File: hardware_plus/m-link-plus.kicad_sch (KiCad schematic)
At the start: 31 parts, among them J3 SIG, J4 PROGRAM, J5 I2C, SW1 RESTORE SETTINGS, U1 AP1117-33, U2 DRV8837C, U3 DRV8837C, U4 ESP-12F, U5 PCA9685PW, U6 DRV8837C

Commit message: Rework M-Link Plus by swapping the PCA9865 and the regulator.
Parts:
- removed R6, R8: 10k, Resistor_SMD:R_0603_1608Metric, symbol Device:R
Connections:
- net CH6: now also U5.15 (LED8); no longer U5.18 (LED11)
- net CH7: now also U5.16 (LED9); no longer U5.17 (LED10)
- net CH8: now also U5.17 (LED10); no longer U5.16 (LED9)
- net CH9: now also U5.18 (LED11); no longer U5.15 (LED8)
- net MTDI: no longer names the net of U4.16 (GPIO15)
- net OE: no longer names the net of U4.17 (GPIO2)
- no-connect marks 16 -> 18
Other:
- note added: "MTDI"
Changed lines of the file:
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@@
   (junction (at 157.48 217.17) (diameter 0) (color 0 0 0 0)
   )
-  (junction (at 184.15 97.79) (diameter 0) (color 0 0 0 0)
-  )
   (junction (at 64.77 262.89) (diameter 0) (color 0 0 0 0)
   )
@@
   )
   (junction (at 97.79 36.83) (diameter 0) (color 0 0 0 0)
-  )
-  (junction (at 189.23 36.83) (diameter 0) (color 0 0 0 0)
   )
   (junction (at 38.1 144.78) (diameter 0) (color 0 0 0 0)
@@
   (no_connect (at 143.51 80.01))
   (no_connect (at 102.87 247.65))
-  (no_connect (at 176.53 80.01))
-  (no_connect (at 176.53 77.47))
+  (no_connect (at 173.99 80.01))
+  (no_connect (at 173.99 77.47))
   (no_connect (at 102.87 245.11))
   (no_connect (at 143.51 74.93))
+  (no_connect (at 173.99 64.77))
   (no_connect (at 102.87 252.73))
   (no_connect (at 143.51 87.63))
   (no_connect (at 143.51 82.55))
+  (no_connect (at 173.99 82.55))
   (no_connect (at 102.87 219.71))
   (no_connect (at 27.94 83.82))
@@
     (stroke (width 0) (type default) (color 0 0 0 0))
   )
-  (wire (pts (xy 199.39 36.83) (xy 189.23 36.83))
-    (stroke (width 0) (type default) (color 0 0 0 0))
-  )
   (wire (pts (xy 27.94 78.74) (xy 30.48 78.74))
     (stroke (width 0) (type default) (color 0 0 0 0))
@@
     (stroke (width 0) (type default) (color 0 0 0 0))
   )
-  (wire (pts (xy 173.99 82.55) (xy 184.15 82.55))
-    (stroke (width 0) (type default) (color 0 0 0 0))
-  )
   (wire (pts (xy 138.43 36.83) (xy 158.75 36.83))
     (stroke (width 0) (type default) (color 0 0 0 0))
@@
     (stroke (width 0) (type default) (color 0 0 0 0))
   )
-  (wire (pts (xy 189.23 46.99) (xy 189.23 64.77))
-    (stroke (width 0) (type default) (color 0 0 0 0))
-  )
   (wire (pts (xy 102.87 36.83) (xy 107.95 36.83))
     (stroke (width 0) (type default) (color 0 0 0 0))
@@
     (stroke (width 0) (type default) (color 0 0 0 0))
   )
-  (wire (pts (xy 173.99 64.77) (xy 189.23 64.77))
-    (stroke (width 0) (type default) (color 0 0 0 0))
-  )
   (wire (pts (xy 30.48 76.2) (xy 30.48 78.74))
     (stroke (width 0) (type default) (color 0 0 0 0))
@@
     (stroke (width 0) (type default) (color 0 0 0 0))
   )
-  (wire (pts (xy 189.23 36.83) (xy 189.23 39.37))
-    (stroke (width 0) (type default) (color 0 0 0 0))
-  )
   (wire (pts (xy 279.4 58.42) (xy 279.4 63.5))
     (stroke (width 0) (type default) (color 0 0 0 0))
@@
     (stroke (width 0) (type default) (color 0 0 0 0))
   )
-  (wire (pts (xy 184.15 95.25) (xy 184.15 97.79))
-    (stroke (width 0) (type default) (color 0 0 0 0))
-  )
   (wire (pts (xy 158.75 36.83) (xy 158.75 54.61))
     (stroke (width 0) (type default) (color 0 0 0 0))
@@
     (stroke (width 0) (type default) (color 0 0 0 0))
   )
-  (wire (pts (xy 158.75 97.79) (xy 184.15 97.79))
+  (wire (pts (xy 158.75 97.79) (xy 199.39 97.79))
     (stroke (width 0) (type default) (color 0 0 0 0))
   )
@@
     (stroke (width 0) (type default) (color 0 0 0 0))
   )
-  (wire (pts (xy 184.15 87.63) (xy 184.15 82.55))
-    (stroke (width 0) (type default) (color 0 0 0 0))
-  )
   (wire (pts (xy 142.24 207.01) (xy 142.24 219.71))
     (stroke (width 0) (type default) (color 0 0 0 0))
@@
     (stroke (width 0) (type default) (color 0 0 0 0))
   )
-  (wire (pts (xy 173.99 77.47) (xy 176.53 77.47))
-    (stroke (width 0) (type default) (color 0 0 0 0))
-  )
   (wire (pts (xy 38.1 137.16) (xy 38.1 144.78))
     (stroke (width 0) (type default) (color 0 0 0 0))
@@
     (stroke (width 0) (type default) (color 0 0 0 0))
   )
-  (wire (pts (xy 179.07 36.83) (xy 189.23 36.83))
+  (wire (pts (xy 179.07 36.83) (xy 199.39 36.83))
     (stroke (width 0) (type default) (color 0 0 0 0))
   )
@@
     (stroke (width 0) (type default) (color 0 0 0 0))
   )
-  (wire (pts (xy 184.15 97.79) (xy 199.39 97.79))
-    (stroke (width 0) (type default) (color 0 0 0 0))
-  )
   (wire (pts (xy 27.94 144.78) (xy 38.1 144.78))
     (stroke (width 0) (type default) (color 0 0 0 0))
   )
-  (wire (pts (xy 173.99 80.01) (xy 176.53 80.01))
-    (stroke (width 0) (type default) (color 0 0 0 0))
-  )
   (wire (pts (xy 62.23 214.63) (xy 67.31 214.63))
     (stroke (width 0) (type default) (color 0 0 0 0))
@@
   )
   (text "FACTORY RESET SWITCH" (at 185.42 59.69 0)
+    (effects (font (size 1.27 1.27)) (justify left bottom))
+  )
+  (text "MTDI" (at 176.53 82.55 0)
     (effects (font (size 1.27 1.27)) (justify left bottom))
   )
@@
     (effects (font (size 1.27 1.27)) (justify left bottom))
   )
-  (label "CH7" (at 107.95 240.03 0)
+  (label "CH7" (at 107.95 237.49 0)
     (effects (font (size 1.27 1.27)) (justify left bottom))
   )
@@
     (effects (font (size 1.27 1.27)) (justify right bottom))
   )
-  (label "MTDI" (at 176.53 82.55 0)
-    (effects (font (size 1.27 1.27)) (justify left bottom))
-  )
   (label "M1B" (at 160.02 240.03 0)
     (effects (font (size 1.27 1.27)) (justify left bottom))
@@
     (effects (font (size 1.27 1.27)) (justify left bottom))
   )
-  (label "CH6" (at 107.95 242.57 0)
+  (label "CH6" (at 107.95 234.95 0)
     (effects (font (size 1.27 1.27)) (justify left bottom))
   )
@@
     (effects (font (size 1.27 1.27)) (justify left bottom))
   )
-  (label "CH9" (at 107.95 234.95 0)
+  (label "CH9" (at 107.95 242.57 0)
     (effects (font (size 1.27 1.27)) (justify left bottom))
   )
@@
     (effects (font (size 1.27 1.27)) (justify left bottom))
   )
-  (label "CH8" (at 107.95 237.49 0)
+  (label "CH8" (at 107.95 240.03 0)
     (effects (font (size 1.27 1.27)) (justify left bottom))
   )
@@
   (label "ADC" (at 140.97 69.85 180)
     (effects (font (size 1.27 1.27)) (justify right bottom))
-  )
-  (label "OE" (at 176.53 64.77 0)
-    (effects (font (size 1.27 1.27)) (justify left bottom))
   )
   (label "RESET" (at 138.43 59.69 180)
@@
     (pin "2")
   )
-  (symbol (lib_id "Device:R") (at 184.15 91.44 0) (unit 1)
-    (in_bom yes) (on_board yes)
-    (property "Reference" "R6" (id 0) (at 185.928 90.2716 0)
-      (effects (font (size 1.27 1.27)) (justify left))
-    )
-    (property "Value" "10k" (id 1) (at 185.928 92.583 0)
-      (effects (font (size 1.27 1.27)) (justify left))
-    )
-    (property "Footprint" "Resistor_SMD:R_0603_1608Metric" (id 2) (at 182.372 91.44 90)
-      (effects (font (size 1.27 1.27)) hide)
-    )
-    (property "Datasheet" "~" (id 3) (at 184.15 91.44 0)
-      (effects (font (size 1.27 1.27)) hide)
-    )
-    (pin "1")
-    (pin "2")
-  )
   (symbol (lib_id "Device:C") (at 199.39 91.44 0) (unit 1)
     (in_bom yes) (on_board yes)
@@
     )
     (pin "1")
-  )
-  (symbol (lib_id "Device:R") (at 189.23 43.18 0) (unit 1)
-    (in_bom yes) (on_board yes)
-    (property "Reference" "R8" (id 0) (at 191.008 42.0116 0)
-      (effects (font (size 1.27 1.27)) (justify left))
-    )
-    (property "Value" "10k" (id 1) (at 191.008 44.323 0)
-      (effects (font (size 1.27 1.27)) (justify left))
-    )
-    (property "Footprint" "Resistor_SMD:R_0603_1608Metric" (id 2) (at 187.452 43.18 90)
-      (effects (font (size 1.27 1.27)) hide)
-    )
-    (property "Datasheet" "~" (id 3) (at 189.23 43.18 0)
-      (effects (font (size 1.27 1.27)) hide)
-    )
-    (pin "1")
-    (pin "2")
   )
   (symbol (lib_id "Driver_LED:PCA9685PW") (at 85.09 232.41 0) (unit 1)
@@
       (reference "R5") (unit 1) (value "10k") (footprint "Resistor_SMD:R_0603_1608Metric")
     )
-    (path "/00000000-0000-0000-0000-0000622ce983"
-      (reference "R6") (unit 1) (value "10k") (footprint "Resistor_SMD:R_0603_1608Metric")
-    )
     (path "/cdafacf6-da16-4628-a51b-2c41b16160e2"
       (reference "R7") (unit 1) (value "4k7") (footprint "Resistor_SMD:R_0603_1608Metric")
     )
-    (path "/39e4b6eb-a1fe-4cb5-a6fd-282a9ff5da5f"
-      (reference "R8") (unit 1) (value "10k") (footprint "Resistor_SMD:R_0603_1608Metric")
-    )
     (path "/aaf746db-d965-486e-9f00-72907204e71b"

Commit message: Add resistors back to GPIO2 and GPIO15.
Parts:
- added R6, R8: 10k, Resistor_SMD:R_0603_1608Metric, symbol Device:R
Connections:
- net +3V3: now also R8.1
- net GND: now also R6.2
- net at U4.16 (GPIO15): now also R6.1
- net at U4.17 (GPIO2): now also R8.2
- no-connect marks 18 -> 16
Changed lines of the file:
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@@
   (junction (at 144.78 247.65) (diameter 0) (color 0 0 0 0)
   )
+  (junction (at 184.15 97.79) (diameter 0) (color 0 0 0 0)
+  )
   (junction (at 64.77 245.11) (diameter 0) (color 0 0 0 0)
   )
@@
   )
   (junction (at 292.1 60.96) (diameter 0) (color 0 0 0 0)
+  )
+  (junction (at 190.5 36.83) (diameter 0) (color 0 0 0 0)
   )
   (junction (at 64.77 242.57) (diameter 0) (color 0 0 0 0)
@@
   (no_connect (at 102.87 245.11))
   (no_connect (at 143.51 74.93))
-  (no_connect (at 173.99 64.77))
   (no_connect (at 102.87 252.73))
   (no_connect (at 143.51 87.63))
   (no_connect (at 143.51 82.55))
-  (no_connect (at 173.99 82.55))
   (no_connect (at 102.87 219.71))
   (no_connect (at 27.94 83.82))
@@
     (stroke (width 0) (type default) (color 0 0 0 0))
   )
+  (wire (pts (xy 173.99 64.77) (xy 190.5 64.77))
+    (stroke (width 0) (type default) (color 0 0 0 0))
+  )
   (wire (pts (xy 144.78 247.65) (xy 144.78 245.11))
     (stroke (width 0) (type default) (color 0 0 0 0))
@@
     (stroke (width 0) (type default) (color 0 0 0 0))
   )
+  (wire (pts (xy 184.15 95.25) (xy 184.15 97.79))
+    (stroke (width 0) (type default) (color 0 0 0 0))
+  )
   (wire (pts (xy 292.1 60.96) (xy 294.64 60.96))
     (stroke (width 0) (type default) (color 0 0 0 0))
@@
     (stroke (width 0) (type default) (color 0 0 0 0))
   )
+  (wire (pts (xy 184.15 87.63) (xy 184.15 82.55))
+    (stroke (width 0) (type default) (color 0 0 0 0))
+  )
   (wire (pts (xy 27.94 137.16) (xy 38.1 137.16))
     (stroke (width 0) (type default) (color 0 0 0 0))
@@
     (stroke (width 0) (type default) (color 0 0 0 0))
   )
+  (wire (pts (xy 190.5 36.83) (xy 199.39 36.83))
+    (stroke (width 0) (type default) (color 0 0 0 0))
+  )
   (wire (pts (xy 27.94 114.3) (xy 30.48 114.3))
     (stroke (width 0) (type default) (color 0 0 0 0))
@@
     (stroke (width 0) (type default) (color 0 0 0 0))
   )
+  (wire (pts (xy 190.5 46.99) (xy 190.5 64.77))
+    (stroke (width 0) (type default) (color 0 0 0 0))
+  )
   (wire (pts (xy 62.23 36.83) (xy 62.23 39.37))
     (stroke (width 0) (type default) (color 0 0 0 0))
@@
     (stroke (width 0) (type default) (color 0 0 0 0))
   )
+  (wire (pts (xy 184.15 97.79) (xy 199.39 97.79))
+    (stroke (width 0) (type default) (color 0 0 0 0))
+  )
   (wire (pts (xy 52.07 34.29) (xy 52.07 36.83))
     (stroke (width 0) (type default) (color 0 0 0 0))
@@
     (stroke (width 0) (type default) (color 0 0 0 0))
   )
+  (wire (pts (xy 190.5 36.83) (xy 190.5 39.37))
+    (stroke (width 0) (type default) (color 0 0 0 0))
+  )
   (wire (pts (xy 22.86 40.64) (xy 22.86 43.18))
     (stroke (width 0) (type default) (color 0 0 0 0))
@@
     (stroke (width 0) (type default) (color 0 0 0 0))
   )
-  (wire (pts (xy 158.75 97.79) (xy 199.39 97.79))
+  (wire (pts (xy 158.75 97.79) (xy 184.15 97.79))
     (stroke (width 0) (type default) (color 0 0 0 0))
   )
@@
     (stroke (width 0) (type default) (color 0 0 0 0))
   )
+  (wire (pts (xy 184.15 82.55) (xy 173.99 82.55))
+    (stroke (width 0) (type default) (color 0 0 0 0))
+  )
   (wire (pts (xy 132.08 229.87) (xy 134.62 229.87))
     (stroke (width 0) (type default) (color 0 0 0 0))
@@
     (stroke (width 0) (type default) (color 0 0 0 0))
   )
-  (wire (pts (xy 179.07 36.83) (xy 199.39 36.83))
+  (wire (pts (xy 179.07 36.83) (xy 190.5 36.83))
     (stroke (width 0) (type default) (color 0 0 0 0))
   )
@@
     (pin "1")
   )
+  (symbol (lib_id "Device:R") (at 184.15 91.44 0) (unit 1)
+    (in_bom yes) (on_board yes) (fields_autoplaced)
+    (property "Reference" "R6" (id 0) (at 186.69 90.1699 0)
+      (effects (font (size 1.27 1.27)) (justify left))
+    )
+    (property "Value" "10k" (id 1) (at 186.69 92.7099 0)
+      (effects (font (size 1.27 1.27)) (justify left))
+    )
+    (property "Footprint" "Resistor_SMD:R_0603_1608Metric" (id 2) (at 182.372 91.44 90)
+      (effects (font (size 1.27 1.27)) hide)
+    )
+    (property "Datasheet" "~" (id 3) (at 184.15 91.44 0)
+      (effects (font (size 1.27 1.27)) hide)
+    )
+    (pin "1")
+    (pin "2")
+  )
   (symbol (lib_id "power:GND") (at 158.75 100.33 0) (unit 1)
     (in_bom yes) (on_board yes)
@@
     (pin "2")
   )
+  (symbol (lib_id "Device:R") (at 190.5 43.18 0) (unit 1)
+    (in_bom yes) (on_board yes) (fields_autoplaced)
+    (property "Reference" "R8" (id 0) (at 193.04 41.9099 0)
+      (effects (font (size 1.27 1.27)) (justify left))
+    )
+    (property "Value" "10k" (id 1) (at 193.04 44.4499 0)
+      (effects (font (size 1.27 1.27)) (justify left))
+    )
+    (property "Footprint" "Resistor_SMD:R_0603_1608Metric" (id 2) (at 188.722 43.18 90)
+      (effects (font (size 1.27 1.27)) hide)
+    )
+    (property "Datasheet" "~" (id 3) (at 190.5 43.18 0)
+      (effects (font (size 1.27 1.27)) hide)
+    )
+    (pin "1")
+    (pin "2")
+  )
   (symbol (lib_id "Device:R") (at 304.8 60.96 180) (unit 1)
     (in_bom yes) (on_board yes) (fields_autoplaced)
@@
       (reference "R5") (unit 1) (value "10k") (footprint "Resistor_SMD:R_0603_1608Metric")
     )
+    (path "/6d11c2b7-5e18-46c4-8c02-fec05a262b22"
+      (reference "R6") (unit 1) (value "10k") (footprint "Resistor_SMD:R_0603_1608Metric")
+    )
     (path "/cdafacf6-da16-4628-a51b-2c41b16160e2"
       (reference "R7") (unit 1) (value "4k7") (footprint "Resistor_SMD:R_0603_1608Metric")
     )
+    (path "/cd0ff163-470d-4898-84b4-5748001022e8"
+      (reference "R8") (unit 1) (value "10k") (footprint "Resistor_SMD:R_0603_1608Metric")
+    )
     (path "/aaf746db-d965-486e-9f00-72907204e71b"

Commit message: Plot M-Link Plus v1.0
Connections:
- net MTDI: now reaches R6.1, U4.16 (GPIO15)
- net ESP_LED: now reaches R8.2, U4.17 (GPIO2)
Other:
- note removed: "MTDI"
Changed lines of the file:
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@@
-    (effects (font (size 1.27 1.27)) (justify left bottom))
-  )
-  (text "MTDI" (at 176.53 82.55 0)
     (effects (font (size 1.27 1.27)) (justify left bottom))
   )
@@
     (effects (font (size 1.27 1.27)) (justify left bottom))
   )
+  (label "ESP_LED" (at 176.53 64.77 0)
+    (effects (font (size 1.27 1.27)) (justify left bottom))
+  )
   (label "SLEEP" (at 132.08 229.87 180)
     (effects (font (size 1.27 1.27)) (justify right bottom))
@@
     (effects (font (size 1.27 1.27)) (justify left bottom))
   )
+  (label "MTDI" (at 176.53 82.55 0)
+    (effects (font (size 1.27 1.27)) (justify left bottom))
+  )

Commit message: Implement feedback path from PCA9865 to an ESP8266 input for timing.
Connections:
- net FEEDBACK: now reaches U5.7 (LED1)
- net FEEDBACK: now also U4.7 (GPIO13)
- no-connect marks 16 -> 14
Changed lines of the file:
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@@
   (no_connect (at 143.51 85.09))
   (no_connect (at 102.87 250.19))
-  (no_connect (at 102.87 217.17))
   (no_connect (at 143.51 80.01))
   (no_connect (at 102.87 247.65))
   (no_connect (at 173.99 80.01))
-  (no_connect (at 173.99 77.47))
-  (no_connect (at 102.87 245.11))
   (no_connect (at 143.51 74.93))
   (no_connect (at 102.87 252.73))
@@
   (no_connect (at 27.94 83.82))
   (no_connect (at 143.51 77.47))
+  (no_connect (at 102.87 245.11))
   (wire (pts (xy 85.09 49.53) (xy 97.79 49.53))
     (stroke (width 0) (type default) (color 0 0 0 0))
@@
     (stroke (width 0) (type default) (color 0 0 0 0))
   )
+  (wire (pts (xy 102.87 217.17) (xy 107.95 217.17))
+    (stroke (width 0) (type default) (color 0 0 0 0))
+  )
   (wire (pts (xy 173.99 67.31) (xy 176.53 67.31))
     (stroke (width 0) (type default) (color 0 0 0 0))
@@
     (stroke (width 0) (type default) (color 0 0 0 0))
   )
+  (wire (pts (xy 173.99 77.47) (xy 176.53 77.47))
+    (stroke (width 0) (type default) (color 0 0 0 0))
+  )
   (wire (pts (xy 279.4 71.12) (xy 279.4 76.2))
     (stroke (width 0) (type default) (color 0 0 0 0))
@@
     (effects (font (size 1.27 1.27)) (justify right bottom))
   )
+  (label "FEEDBACK" (at 176.53 77.47 0)
+    (effects (font (size 1.27 1.27)) (justify left bottom))
+  )
   (label "TX" (at 176.53 67.31 0)
     (effects (font (size 1.27 1.27)) (justify left bottom))
@@
     (effects (font (size 1.27 1.27)) (justify left bottom))
   )
+  (label "FEEDBACK" (at 107.95 217.17 0)
+    (effects (font (size 1.27 1.27)) (justify left bottom))
+  )

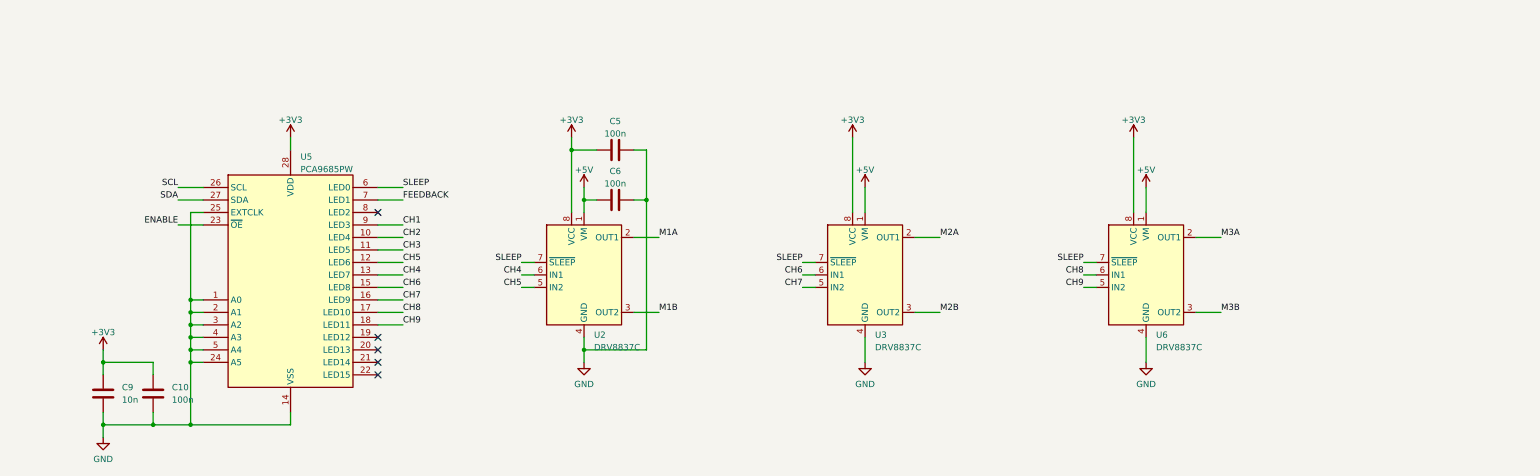
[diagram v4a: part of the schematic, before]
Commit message: Begin rework to add an optional fourth channel.
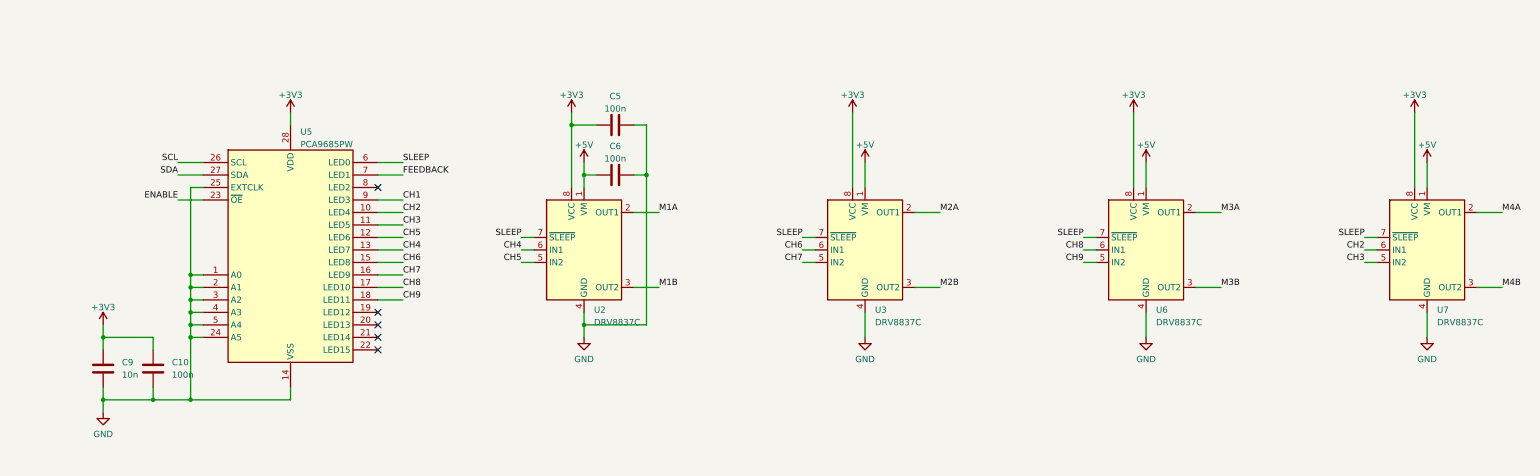
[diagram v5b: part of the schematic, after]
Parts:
- added U7: DRV8837C, Package_SON:WSON-8-1EP_2x2mm_P0.5mm_EP0.9x1.6mm, symbol Driver_Motor:DRV8837C
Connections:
- net +3V3: now also U7.8 (VCC)
- net +5V: now also U7.1 (VM)
- net CH2: now also U7.6 (IN1)
- net CH3: now also U7.5 (IN2)
- net GND: now also U7.4 (GND), U7.9 (GND)
- net SLEEP: now also U7.7 (~{SLEEP})
- new net M4A: U7.2 (OUT1)
- new net M4B: U7.3 (OUT2)
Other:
- moved on the sheet: C10, C5, C6, C9, U2, U3, U5, U6
